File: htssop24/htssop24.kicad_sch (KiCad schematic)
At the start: 3 parts, among them J1 Conn_01x12, J2 Conn_02x12_Counter_Clockwise, J3 Conn_01x12

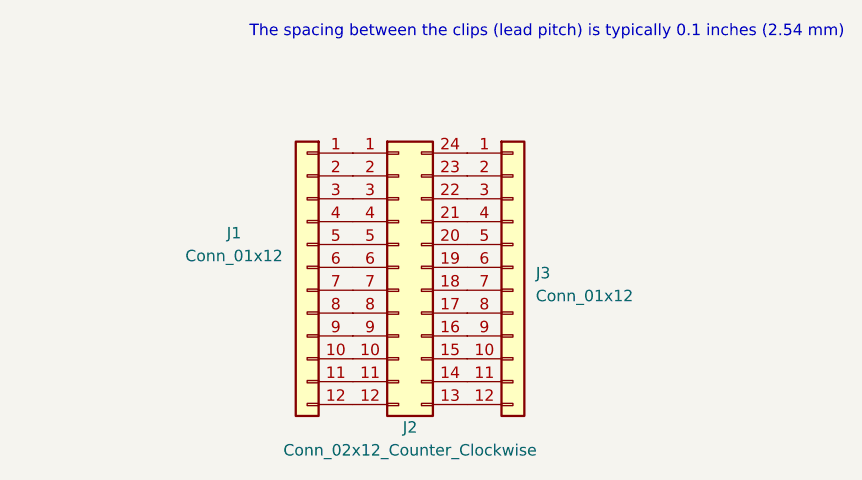
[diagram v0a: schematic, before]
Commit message: gerber file for htssop24
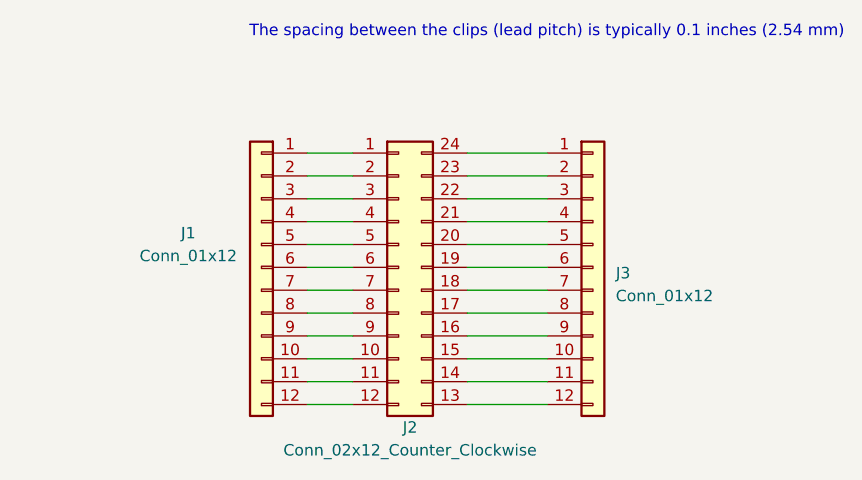
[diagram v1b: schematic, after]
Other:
- moved on the sheet: J1, J3
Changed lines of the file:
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@@
 (kicad_sch (version 20210406) (generator eeschema)
   (paper "A4")
+  (wire (pts (xy 119.38 63.5) (xy 124.46 63.5))
+    (stroke (width 0) (type solid) (color 0 0 0 0))
+  )
+  (wire (pts (xy 119.38 66.04) (xy 124.46 66.04))
+    (stroke (width 0) (type solid) (color 0 0 0 0))
+  )
+  (wire (pts (xy 119.38 68.58) (xy 124.46 68.58))
+    (stroke (width 0) (type solid) (color 0 0 0 0))
+  )
+  (wire (pts (xy 119.38 71.12) (xy 124.46 71.12))
+    (stroke (width 0) (type solid) (color 0 0 0 0))
+  )
+  (wire (pts (xy 119.38 73.66) (xy 124.46 73.66))
+    (stroke (width 0) (type solid) (color 0 0 0 0))
+  )
+  (wire (pts (xy 119.38 76.2) (xy 124.46 76.2))
+    (stroke (width 0) (type solid) (color 0 0 0 0))
+  )
+  (wire (pts (xy 119.38 78.74) (xy 124.46 78.74))
+    (stroke (width 0) (type solid) (color 0 0 0 0))
+  )
+  (wire (pts (xy 119.38 81.28) (xy 124.46 81.28))
+    (stroke (width 0) (type solid) (color 0 0 0 0))
+  )
+  (wire (pts (xy 119.38 83.82) (xy 124.46 83.82))
+    (stroke (width 0) (type solid) (color 0 0 0 0))
+  )
+  (wire (pts (xy 119.38 86.36) (xy 124.46 86.36))
+    (stroke (width 0) (type solid) (color 0 0 0 0))
+  )
+  (wire (pts (xy 119.38 88.9) (xy 124.46 88.9))
+    (stroke (width 0) (type solid) (color 0 0 0 0))
+  )
+  (wire (pts (xy 119.38 91.44) (xy 124.46 91.44))
+    (stroke (width 0) (type solid) (color 0 0 0 0))
+  )
+  (wire (pts (xy 137.16 63.5) (xy 146.05 63.5))
+    (stroke (width 0) (type solid) (color 0 0 0 0))
+  )
+  (wire (pts (xy 137.16 66.04) (xy 146.05 66.04))
+    (stroke (width 0) (type solid) (color 0 0 0 0))
+  )
+  (wire (pts (xy 137.16 68.58) (xy 146.05 68.58))
+    (stroke (width 0) (type solid) (color 0 0 0 0))
+  )
+  (wire (pts (xy 137.16 71.12) (xy 146.05 71.12))
+    (stroke (width 0) (type solid) (color 0 0 0 0))
+  )
+  (wire (pts (xy 137.16 73.66) (xy 146.05 73.66))
+    (stroke (width 0) (type solid) (color 0 0 0 0))
+  )
+  (wire (pts (xy 137.16 76.2) (xy 146.05 76.2))
+    (stroke (width 0) (type solid) (color 0 0 0 0))
+  )
+  (wire (pts (xy 137.16 78.74) (xy 146.05 78.74))
+    (stroke (width 0) (type solid) (color 0 0 0 0))
+  )
+  (wire (pts (xy 137.16 81.28) (xy 146.05 81.28))
+    (stroke (width 0) (type solid) (color 0 0 0 0))
+  )
+  (wire (pts (xy 137.16 83.82) (xy 146.05 83.82))
+    (stroke (width 0) (type solid) (color 0 0 0 0))
+  )
+  (wire (pts (xy 137.16 86.36) (xy 146.05 86.36))
+    (stroke (width 0) (type solid) (color 0 0 0 0))
+  )
+  (wire (pts (xy 137.16 88.9) (xy 146.05 88.9))
+    (stroke (width 0) (type solid) (color 0 0 0 0))
+  )
+  (wire (pts (xy 137.16 91.44) (xy 146.05 91.44))
+    (stroke (width 0) (type solid) (color 0 0 0 0))
+  )
   (text "The spacing between the clips (lead pitch) is typically 0.1 inches (2.54 mm)"
     (at 179.07 50.8 0)
     (effects (font (size 1.27 1.27)) (justify right bottom))
   )
-  (symbol (lib_id "Connector_Generic:Conn_01x12") (at 119.38 76.2 0) (mirror y) (unit 1)
+  (symbol (lib_id "Connector_Generic:Conn_01x12") (at 114.3 76.2 0) (mirror y) (unit 1)
     (in_bom yes) (on_board yes)
-    (property "Reference" "J1" (id 0) (at 111.252 72.39 0))
-    (property "Value" "Conn_01x12" (id 1) (at 111.252 74.93 0))
-    (property "Footprint" "Connector_PinHeader_2.54mm:PinHeader_1x12_P2.54mm_Vertical" (id 2) (at 119.38 76.2 0)
+    (property "Reference" "J1" (id 0) (at 106.172 72.39 0))
+    (property "Value" "Conn_01x12" (id 1) (at 106.172 74.93 0))
+    (property "Footprint" "Connector_PinHeader_2.54mm:PinHeader_1x12_P2.54mm_Vertical" (id 2) (at 114.3 76.2 0)
       (effects (font (size 1.27 1.27)) hide)
     )
-    (property "Datasheet" "~" (id 3) (at 119.38 76.2 0)
+    (property "Datasheet" "~" (id 3) (at 114.3 76.2 0)
       (effects (font (size 1.27 1.27)) hide)
     )
@@
     (pin "9")
   )
-  (symbol (lib_id "Connector_Generic:Conn_01x12") (at 142.24 76.2 0) (unit 1)
+  (symbol (lib_id "Connector_Generic:Conn_01x12") (at 151.13 76.2 0) (unit 1)
     (in_bom yes) (on_board yes) (fields_autoplaced)
-    (property "Reference" "J3" (id 0) (at 144.78 76.8349 0)
+    (property "Reference" "J3" (id 0) (at 153.67 76.8349 0)
       (effects (font (size 1.27 1.27)) (justify left))
     )
-    (property "Value" "Conn_01x12" (id 1) (at 144.78 79.3749 0)
+    (property "Value" "Conn_01x12" (id 1) (at 153.67 79.3749 0)
       (effects (font (size 1.27 1.27)) (justify left))
     )
-    (property "Footprint" "Connector_PinHeader_2.54mm:PinHeader_1x12_P2.54mm_Vertical" (id 2) (at 142.24 76.2 0)
+    (property "Footprint" "Connector_PinHeader_2.54mm:PinHeader_1x12_P2.54mm_Vertical" (id 2) (at 151.13 76.2 0)
       (effects (font (size 1.27 1.27)) hide)
     )
-    (property "Datasheet" "~" (id 3) (at 142.24 76.2 0)
+    (property "Datasheet" "~" (id 3) (at 151.13 76.2 0)
       (effects (font (size 1.27 1.27)) hide)
     )
